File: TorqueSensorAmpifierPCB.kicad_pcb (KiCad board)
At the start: 2 copper layers, 25 x 25 mm, 17 parts, among them J1 Conn_01x04_Socket, J2 Conn_01x04_Socket, U1 LM386

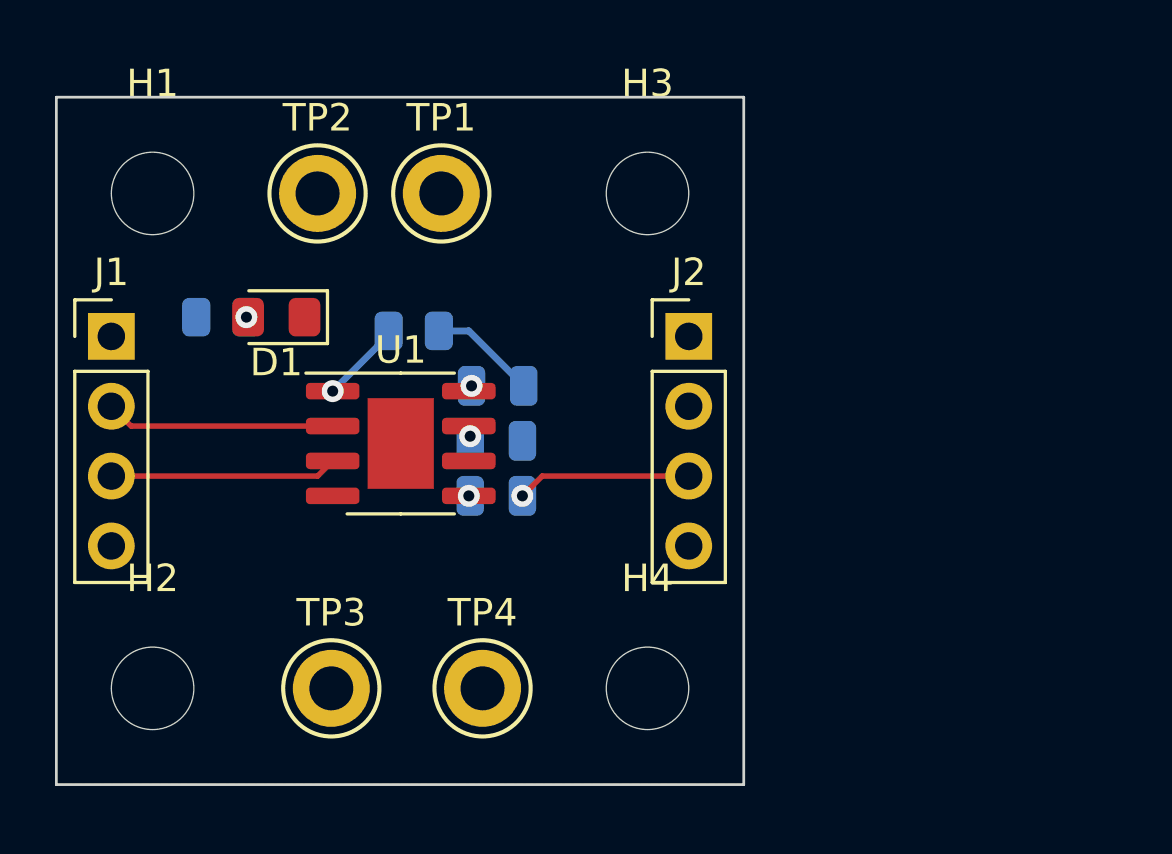
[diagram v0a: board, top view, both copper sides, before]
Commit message: Added torque schematic
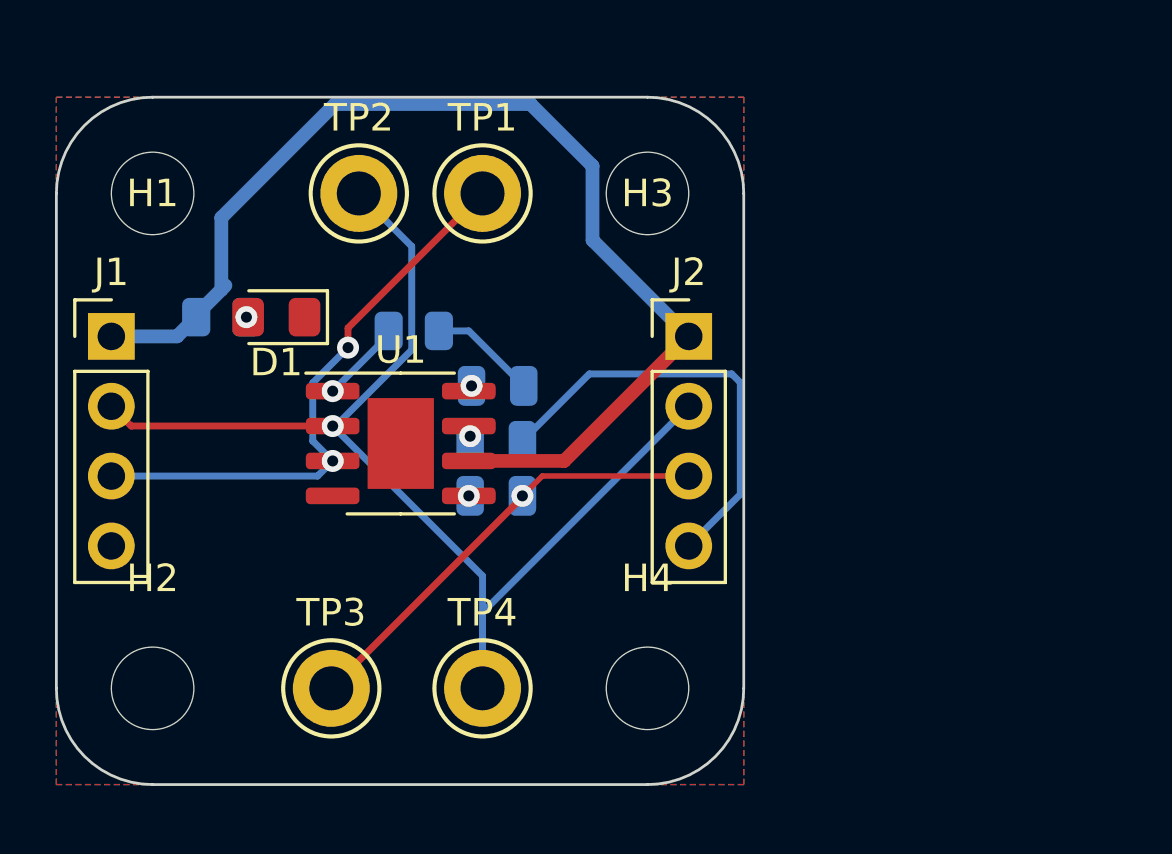
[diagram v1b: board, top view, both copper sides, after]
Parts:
- moved TP1 1.50 mm to (73.0, 91.5)
- moved TP2 1.50 mm to (68.5, 91.5)
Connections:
- J1 pad 2: /SIG_IN_- -> GNDS
- J2 pad 2: /SIG_OUT_- -> GNDS
- TP2 pad 1: /SIG_IN_- -> GNDS
- TP4 pad 1: /SIG_OUT_- -> GNDS
- U1 pad 2: /SIG_IN_- -> GNDS
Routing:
- net GNDS: track 0.00 -> 44.0 mm, vias 0 -> 1
- net +5V: track 0.00 -> 41.3 mm
- net GND: track 0.00 -> 15.8 mm
- net /SIG_IN_+: track 8.28 -> 20.9 mm, vias 0 -> 2
- net /SIG_OUT_+: track 6.35 -> 16.2 mm
- net /SIG_IN_-: track 8.35 -> 0.00 mm
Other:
- outline, holes or cut-outs redrawn
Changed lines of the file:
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@@
   (net 7 "Net-(D1-A)")
   (net 8 "Net-(R2-Pad1)")
-  (net 9 "/SIG_IN_-")
+  (net 9 "GNDS")
   (net 10 "/SIG_IN_+")
   (net 11 "+5V")
-  (net 12 "/SIG_OUT_-")
   (footprint "MountingHole:MountingHole_3mm" (layer "F.Cu")
     (at 79 91.5)
@@
     (property "ki_keywords" "mounting hole")
     (attr exclude_from_pos_files)
-    (fp_text reference "H3" (at 0 -4) (layer "F.SilkS")
+    (fp_text reference "H3" (at 0 0) (layer "F.SilkS")
         (effects (font (size 1 1) (thickness 0.15)))
     )
@@
   )
   (footprint "TestPoint:TestPoint_Keystone_5005-5009_Compact" (layer "F.Cu")
-    (at 71.5 91.5)
+    (at 73 91.5)
     (descr "Keystone Miniature THM Test Point 5005-5009, http://www.keyelco.com/product-pdf.cfm?p=1314")
     (tags "Through Hole Mount Test Points")
@@
       (net 11 "+5V") (pinfunction "Pin_1") (pintype "passive"))
     (pad "2" thru_hole oval (at 0 2.54) (size 1.7 1.7) (drill 1) (layers "*.Cu" "*.Mask")
-      (net 12 "/SIG_OUT_-") (pinfunction "Pin_2") (pintype "passive"))
+      (net 9 "GNDS") (pinfunction "Pin_2") (pintype "passive"))
     (pad "3" thru_hole oval (at 0 5.08) (size 1.7 1.7) (drill 1) (layers "*.Cu" "*.Mask")
       (net 6 "/SIG_OUT_+") (pinfunction "Pin_3") (pintype "passive"))
@@
       (stroke (width 0.15) (type solid)) (fill none) (layer "F.Fab"))
     (pad "1" thru_hole circle (at 0 0) (size 2.8 2.8) (drill 1.6) (layers "*.Cu" "*.Mask")
-      (net 12 "/SIG_OUT_-") (pinfunction "1") (pintype "passive"))
+      (net 9 "GNDS") (pinfunction "1") (pintype "passive"))
     (model "${KICAD6_3DMODEL_DIR}/TestPoint.3dshapes/TestPoint_Keystone_5005-5009_Compact.wrl"
       (offset (xyz 0 0 0))
@@
       (net 8 "Net-(R2-Pad1)") (pinfunction "GAIN") (pintype "input"))
     (pad "2" smd roundrect (at -2.475 -0.635) (size 1.95 0.6) (layers "F.Cu" "F.Paste" "F.Mask") (roundrect_rratio 0.25)
-      (net 9 "/SIG_IN_-") (pinfunction "-") (pintype "input"))
+      (net 9 "GNDS") (pinfunction "-") (pintype "input"))
     (pad "3" smd roundrect (at -2.475 0.635) (size 1.95 0.6) (layers "F.Cu" "F.Paste" "F.Mask") (roundrect_rratio 0.25)
       (net 10 "/SIG_IN_+") (pinfunction "+") (pintype "input"))
@@
   )
   (footprint "TestPoint:TestPoint_Keystone_5005-5009_Compact" (layer "F.Cu")
-    (at 67 91.5)
+    (at 68.5 91.5)
     (descr "Keystone Miniature THM Test Point 5005-5009, http://www.keyelco.com/product-pdf.cfm?p=1314")
     (tags "Through Hole Mount Test Points")
@@
       (stroke (width 0.15) (type solid)) (fill none) (layer "F.Fab"))
     (pad "1" thru_hole circle (at 0 0) (size 2.8 2.8) (drill 1.6) (layers "*.Cu" "*.Mask")
-      (net 9 "/SIG_IN_-") (pinfunction "1") (pintype "passive"))
+      (net 9 "GNDS") (pinfunction "1") (pintype "passive"))
     (model "${KICAD6_3DMODEL_DIR}/TestPoint.3dshapes/TestPoint_Keystone_5005-5009_Compact.wrl"
       (offset (xyz 0 0 0))
@@
       (net 11 "+5V") (pinfunction "Pin_1") (pintype "passive"))
     (pad "2" thru_hole oval (at 0 2.54) (size 1.7 1.7) (drill 1) (layers "*.Cu" "*.Mask")
-      (net 9 "/SIG_IN_-") (pinfunction "Pin_2") (pintype "passive"))
+      (net 9 "GNDS") (pinfunction "Pin_2") (pintype "passive"))
     (pad "3" thru_hole oval (at 0 5.08) (size 1.7 1.7) (drill 1) (layers "*.Cu" "*.Mask")
       (net 10 "/SIG_IN_+") (pinfunction "Pin_3") (pintype "passive"))
@@
     (property "ki_keywords" "mounting hole")
     (attr exclude_from_pos_files)
-    (fp_text reference "H1" (at 0 -4) (layer "F.SilkS")
+    (fp_text reference "H1" (at 0 0) (layer "F.SilkS")
         (effects (font (size 1 1) (thickness 0.15)))
     )
@@
     )
   )
-  (gr_rect (start 57.5 88) (end 82.5 113)
-    (stroke (width 0.1) (type default)) (fill none) (layer "Edge.Cuts"))
+  (gr_arc (start 57.5 91.5) (mid 58.525126 89.025126) (end 61 88)
+    (stroke (width 0.1) (type default)) (layer "Edge.Cuts"))
+  (gr_line (start 79 113) (end 61 113)
+    (stroke (width 0.1) (type default)) (layer "Edge.Cuts"))
+  (gr_arc (start 61 113) (mid 58.525126 111.974874) (end 57.5 109.5)
+    (stroke (width 0.1) (type default)) (layer "Edge.Cuts"))
+  (gr_line (start 57.5 109.5) (end 57.5 91.5)
+    (stroke (width 0.1) (type default)) (layer "Edge.Cuts"))
+  (gr_line (start 61 88) (end 79 88)
+    (stroke (width 0.1) (type default)) (layer "Edge.Cuts"))
+  (gr_line (start 82.5 91.5) (end 82.5 109.5)
+    (stroke (width 0.1) (type default)) (layer "Edge.Cuts"))
+  (gr_arc (start 82.5 109.5) (mid 81.474874 111.974874) (end 79 113)
+    (stroke (width 0.1) (type default)) (layer "Edge.Cuts"))
+  (gr_arc (start 79 88) (mid 81.474874 89.025126) (end 82.5 91.5)
+    (stroke (width 0.1) (type default)) (layer "Edge.Cuts"))
   (segment (start 72.5 100.2805) (end 72.55 100.3305) (width 0.25) (layer "F.Cu") (net 1))
   (segment (start 72.5 99.96) (end 72.5 100.2805) (width 0.25) (layer "F.Cu") (net 1))
   (via (at 72.55 100.3305) (size 0.8) (drill 0.4) (layers "F.Cu" "B.Cu") (net 1))
+  (segment (start 82.065 98.065) (end 82.375 98.375) (width 0.25) (layer "B.Cu") (net 2))
+  (segment (start 82.375 98.375) (end 82.375 102.445) (width 0.25) (layer "B.Cu") (net 2))
+  (segment (start 74.45 100.5) (end 76.885 98.065) (width 0.25) (layer "B.Cu") (net 2))
+  (segment (start 76.885 98.065) (end 82.065 98.065) (width 0.25) (layer "B.Cu") (net 2))
+  (segment (start 82.375 102.445) (end 80.5 104.32) (width 0.25) (layer "B.Cu") (net 2))
   (segment (start 72.5 98.6) (end 72.6 98.5) (width 0.25) (layer "F.Cu") (net 3))
   (segment (start 72.5 98.69) (end 72.5 98.6) (width 0.25) (layer "F.Cu") (net 3))
@@
   (via (at 72.5 102.5) (size 0.8) (drill 0.4) (layers "F.Cu" "B.Cu") (net 5))
   (segment (start 72.55 102.5) (end 72.5 102.5) (width 0.25) (layer "B.Cu") (net 5))
+  (segment (start 74.45 102.55) (end 74.45 102.5) (width 0.25) (layer "F.Cu") (net 6))
   (segment (start 80.5 101.78) (end 75.17 101.78) (width 0.2) (layer "F.Cu") (net 6))
+  (segment (start 67.5 109.5) (end 74.45 102.55) (width 0.25) (layer "F.Cu") (net 6))
   (segment (start 75.17 101.78) (end 74.45 102.5) (width 0.2) (layer "F.Cu") (net 6))
   (via (at 74.45 102.5) (size 0.8) (drill 0.4) (layers "F.Cu" "B.Cu") (net 6))
@@
   (segment (start 69.5875 96.5) (end 69.5875 96.6525) (width 0.25) (layer "B.Cu") (net 8))
   (segment (start 69.5875 96.6525) (end 67.55 98.69) (width 0.25) (layer "B.Cu") (net 8))
-  (segment (start 67.55 99.96) (end 60.22 99.96) (width 0.2) (layer "F.Cu") (net 9))
-  (segment (start 60.22 99.96) (end 59.5 99.24) (width 0.2) (layer "F.Cu") (net 9))
-  (segment (start 59.5 101.78) (end 67 101.78) (width 0.2) (layer "F.Cu") (net 10))
-  (segment (start 67 101.78) (end 67.55 101.23) (width 0.2) (layer "F.Cu") (net 10))
+  (segment (start 67.55 99.96) (end 60.22 99.96) (width 0.25) (layer "F.Cu") (net 9))
+  (segment (start 60.22 99.96) (end 59.5 99.24) (width 0.25) (layer "F.Cu") (net 9))
+  (via (at 67.55 99.96) (size 0.8) (drill 0.4) (layers "F.Cu" "B.Cu") (net 9))
+  (segment (start 70.425 97.188173) (end 67.653173 99.96) (width 0.25) (layer "B.Cu") (net 9))
+  (segment (start 73 109.5) (end 73 106.74) (width 0.25) (layer "B.Cu") (net 9))
+  (segment (start 68.5 91.5) (end 70.425 93.425) (width 0.25) (layer "B.Cu") (net 9))
+  (segment (start 73 105.41) (end 67.55 99.96) (width 0.25) (layer "B.Cu") (net 9))
+  (segment (start 70.425 93.425) (end 70.425 97.188173) (width 0.25) (layer "B.Cu") (net 9))
+  (segment (start 73 109.5) (end 73 105.41) (width 0.25) (layer "B.Cu") (net 9))
+  (segment (start 67.653173 99.96) (end 67.55 99.96) (width 0.25) (layer "B.Cu") (net 9))
+  (segment (start 73 106.74) (end 80.5 99.24) (width 0.25) (layer "B.Cu") (net 9))
+  (segment (start 68.107701 96.392299) (end 73 91.5) (width 0.25) (layer "F.Cu") (net 10))
+  (segment (start 68.107701 97.107701) (end 68.107701 96.392299) (width 0.25) (layer "F.Cu") (net 10))
+  (via (at 67.55 101.23) (size 0.8) (drill 0.4) (layers "F.Cu" "B.Cu") (net 10))
+  (via (at 68.107701 97.107701) (size 0.8) (drill 0.4) (layers "F.Cu" "B.Cu") (net 10))
+  (segment (start 59.5 101.78) (end 67 101.78) (width 0.25) (layer "B.Cu") (net 10))
+  (segment (start 68.107701 97.107701) (end 66.825 98.390402) (width 0.25) (layer "B.Cu") (net 10))
+  (segment (start 66.825 100.505) (end 67.55 101.23) (width 0.25) (layer "B.Cu") (net 10))
+  (segment (start 66.825 98.390402) (end 66.825 100.505) (width 0.25) (layer "B.Cu") (net 10))
+  (segment (start 67 101.78) (end 67.55 101.23) (width 0.25) (layer "B.Cu") (net 10))
+  (segment (start 72.5 101.23) (end 75.97 101.23) (width 0.5) (layer "F.Cu") (net 11))
+  (segment (start 75.97 101.23) (end 80.5 96.7) (width 0.5) (layer "F.Cu") (net 11))
+  (segment (start 61.8875 96.7) (end 59.5 96.7) (width 0.5) (layer "B.Cu") (net 11))
+  (segment (start 62.5875 96) (end 61.8875 96.7) (width 0.5) (layer "B.Cu") (net 11))
+  (segment (start 62.5875 96) (end 62.5875 95.9125) (width 0.5) (layer "B.Cu") (net 11))
+  (segment (start 77 93.2) (end 80.5 96.7) (width 0.5) (layer "B.Cu") (net 11))
+  (segment (start 77 90.5) (end 77 93.2) (width 0.5) (layer "B.Cu") (net 11))
+  (segment (start 63.5 92.383704) (end 67.633704 88.25) (width 0.5) (layer "B.Cu") (net 11))
+  (segment (start 63.5 95) (end 63.65 94.85) (width 0.5) (layer "B.Cu") (net 11))
+  (segment (start 62.5875 95.9125) (end 63.5 95) (width 0.5) (layer "B.Cu") (net 11))
+  (segment (start 74.75 88.25) (end 77 90.5) (width 0.5) (layer "B.Cu") (net 11))
+  (segment (start 63.5 95) (end 63.5 92.383704) (width 0.5) (layer "B.Cu") (net 11))
+  (segment (start 67.633704 88.25) (end 74.75 88.25) (width 0.5) (layer "B.Cu") (net 11))
   (zone (net 2) (net_name "GND") (layers "F&B.Cu") (hatch edge 0.5)
     (connect_pads (clearance 0.5))

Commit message: Added Gerbers
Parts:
- removed R1: R, Resistor_SMD:R_0805_2012Metric
- added C4: .05uF, Capacitor_SMD:C_0805_2012Metric, F.Cu at (94.6, 101.0)
- added R3: 10, Resistor_SMD:R_0805_2012Metric, F.Cu at (94.6, 104.0)
- C1: moved to F.Cu
- C2: value C -> 10uF; moved to F.Cu
- C3: value C -> 250uF; moved to F.Cu
- R2: value R -> 1.2k; moved to F.Cu
- U1: footprint Package_SO:SOIC-8-1EP_3.9x4.9mm_P1.27mm_EP2.41x3.3mm -> HCRL:M08A_TEX-L
- moved C1 2.45 mm to (76.0, 100.5)
- moved C2 2.45 mm to (76.0, 98.5)
- moved C3 2.45 mm to (76.0, 102.5)
- moved D1 2.00 mm to (67.5, 96.0)
- moved R2 1.00 mm to (71.5, 96.5), turned to 180 degrees
- moved TP2 1.00 mm to (67.5, 91.5)
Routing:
- net GND: track 15.8 -> 0.00 mm
- net +5V: track 41.3 -> 26.4 mm, vias 0 -> 2
- net GNDS: track 44.0 -> 36.0 mm
- net Net-(C2-Pad2): track 3.92 -> 8.04 mm
- net Net-(R2-Pad1): track 3.03 -> 6.10 mm, vias 1 -> 2
- net Net-(C2-Pad1): track 0.23 -> 2.57 mm, vias 1 -> 0
- net Net-(C3-Pad1): track 0.05 -> 2.35 mm, vias 1 -> 0
- net Net-(U1-BYPASS): track 0.39 -> 2.58 mm, vias 1 -> 0
- net Net-(D1-A): track 0.06 -> 2.06 mm, vias 1 -> 0
- net /SIG_IN_+: track 20.9 -> 20.3 mm, vias 2 -> 1
- net /SIG_OUT_+: vias 1 -> 0
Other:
- board text added: "5V"
- board text added: "GND"
- board text added: "In_+"
- board text added: "In_-"
- board text added: "SIG_IN_+"
- board text added: "SIG_OUT_+"

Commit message: Added BOMs
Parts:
- added R1: 5k, Resistor_SMD:R_0805_2012Metric, F.Cu at (63.6, 96.0)
- C1: value C -> 1uF
- moved R3 23.2 mm to (71.4, 105.0)
- moved C4 18.1 mm to (77.0, 105.0)
- moved R2 0.50 mm to (71.5, 96.0)
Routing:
- net GNDS: track 36.0 -> 45.4 mm
- net Net-(C4-Pad1): track 0.00 -> 3.83 mm, vias 0 -> 2
- net Net-(C3-Pad1): track 2.35 -> 5.74 mm
- net Net-(C2-Pad2): track 8.04 -> 8.75 mm
